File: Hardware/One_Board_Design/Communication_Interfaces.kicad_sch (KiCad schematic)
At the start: 51 parts, among them Q2 2SD882, Q5 2SD882, Q6 2SD882, U1 TCAN3414DR, U10 LTV-356T, U11 LTV-356T, U12 LTV-356T, U14 LTV-356T, U3 MAX3485, U6 LTV-356T

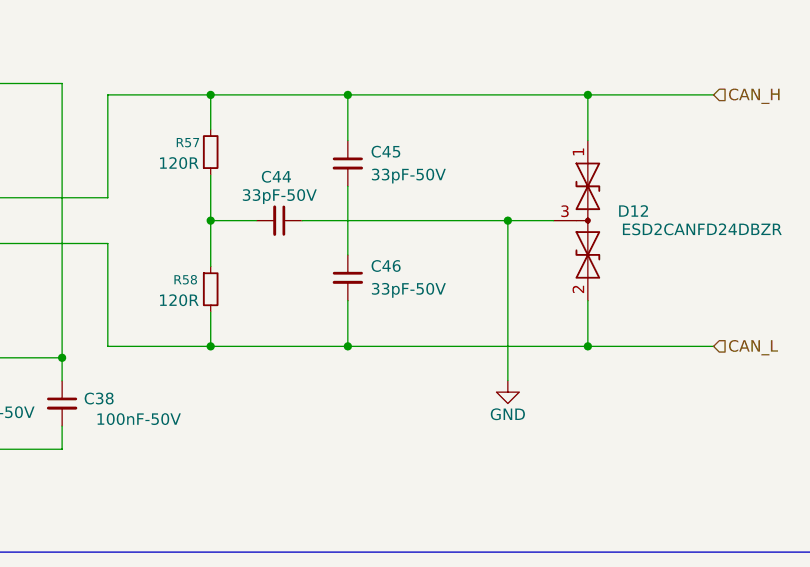
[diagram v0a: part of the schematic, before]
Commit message: refactor(hardware): move KiCad project into One_Board_Design/
Relocate the single-board KiCad project (root schematic, five hierarchical sheets, PCB, project file, and library tables) into Hardware/One_Board_Design/ so the shared symbols, footprints, and 3D models stay in Hardware/libraries/.

Update library tables and 3D model references to use \/../libraries/... so the moved project resolves the shared library location correctly. Replace SparkFun symbol references with the equivalent KiCad standard symbols. Add One_Board_Design README documenting the shared-library layout.

Ultraworked with [Sisyphus](https://github.com/code-yeongyu/oh-my-openagent)

Co-authored-by: Sisyphus <clio-agent@sisyphuslabs.ai>
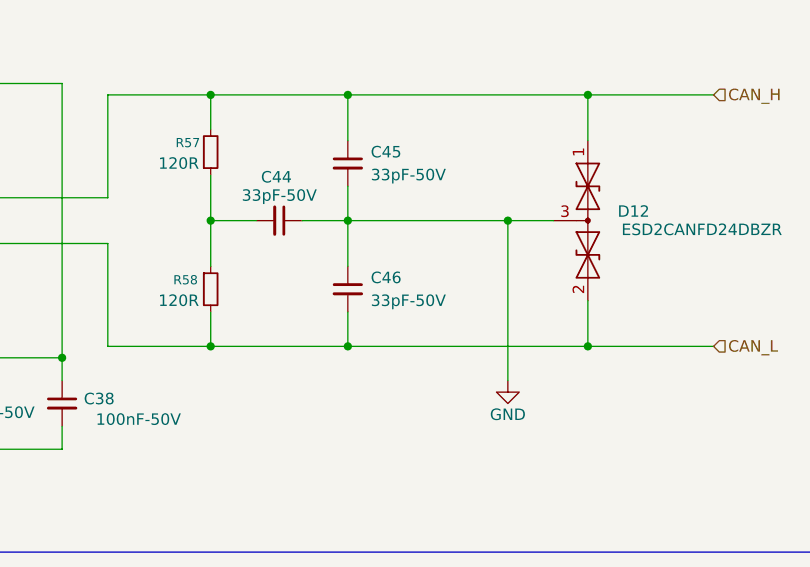
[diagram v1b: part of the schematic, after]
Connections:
- net GND: now also C45.2, C46.1
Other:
- moved on the sheet: C46
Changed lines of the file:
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@@
 	)
 	(junction
-		(at 215.9 58.42)
-		(diameter 0)
-		(color 0 0 0 0)
-	)
-	(junction
 		(at 160.02 97.79)
 		(diameter 0)
@@
 	)
 	(junction
+		(at 233.68 44.45)
+		(diameter 0)
+		(color 0 0 0 0)
+	)
+	(junction
 		(at 256.54 156.21)
 		(diameter 0)
@@
 	)
 	(junction
-		(at 233.68 44.45)
+		(at 82.55 99.06)
 		(diameter 0)
 		(color 0 0 0 0)
 	)
 	(junction
-		(at 82.55 99.06)
+		(at 215.9 58.42)
 		(diameter 0)
 		(color 0 0 0 0)
@@
 	)
 	(junction
+		(at 215.9 44.45)
+		(diameter 0)
+		(color 0 0 0 0)
+	)
+	(junction
 		(at 242.57 58.42)
 		(diameter 0)
@@
 	(wire
 		(pts
-			(xy 215.9 58.42) (xy 215.9 53.34)
+			(xy 215.9 58.42) (xy 215.9 54.61)
 		)
 		(stroke
@@
 	(wire
 		(pts
-			(xy 215.9 40.64) (xy 215.9 48.26)
-		)
-		(stroke
-			(width 0)
-			(type default)
-		)
-	)
-	(wire
-		(pts
 			(xy 161.29 158.75) (xy 161.29 161.29)
 		)
@@
 	(wire
 		(pts
-			(xy 233.68 44.45) (xy 233.68 62.23)
-		)
-		(stroke
-			(width 0)
-			(type default)
-		)
-	)
-	(wire
-		(pts
 			(xy 71.12 163.83) (xy 71.12 167.64)
 		)
@@
 	(wire
 		(pts
-			(xy 168.91 62.23) (xy 168.91 59.69)
+			(xy 233.68 44.45) (xy 238.76 44.45)
 		)
 		(stroke
@@
 	(wire
 		(pts
-			(xy 160.02 110.49) (xy 165.1 110.49)
+			(xy 168.91 62.23) (xy 168.91 59.69)
 		)
 		(stroke
@@
 	(wire
 		(pts
-			(xy 210.82 44.45) (xy 233.68 44.45)
+			(xy 160.02 110.49) (xy 165.1 110.49)
 		)
 		(stroke
@@
 	(wire
 		(pts
-			(xy 233.68 44.45) (xy 238.76 44.45)
+			(xy 210.82 44.45) (xy 215.9 44.45)
 		)
 		(stroke
@@
 	(wire
 		(pts
+			(xy 233.68 62.23) (xy 233.68 44.45)
+		)
+		(stroke
+			(width 0)
+			(type default)
+		)
+	)
+	(wire
+		(pts
 			(xy 48.26 30.48) (xy 48.26 34.29)
 		)
@@
 	(wire
 		(pts
+			(xy 215.9 44.45) (xy 233.68 44.45)
+		)
+		(stroke
+			(width 0)
+			(type default)
+		)
+	)
+	(wire
+		(pts
 			(xy 161.29 134.62) (xy 161.29 138.43)
 		)
@@
 	(wire
 		(pts
+			(xy 215.9 40.64) (xy 215.9 44.45)
+		)
+		(stroke
+			(width 0)
+			(type default)
+		)
+	)
+	(wire
+		(pts
 			(xy 226.06 140.97) (xy 234.95 140.97)
 		)
@@
 	(wire
 		(pts
+			(xy 215.9 44.45) (xy 215.9 49.53)
+		)
+		(stroke
+			(width 0)
+			(type default)
+		)
+	)
+	(wire
+		(pts
 			(xy 138.43 91.44) (xy 148.59 91.44)
 		)
@@
 	(symbol
 		(lib_id "Device:C_Small")
-		(at 215.9 50.8 0)
+		(at 215.9 52.07 0)
 		(unit 1)
 		(body_style 1)
@@
 		(dnp no)
 		(property "Reference" "C46"
-			(at 218.44 49.5362 0)
+			(at 218.44 50.8062 0)
 			(show_name no)
 			(do_not_autoplace no)
@@
 		)
 		(property "Value" "33pF-50V"
-			(at 218.44 52.0762 0)
+			(at 218.44 53.3462 0)
 			(show_name no)
 			(do_not_autoplace no)
@@
 		)
 		(property "Footprint" "Capacitor_SMD:C_0603_1608Metric"
-			(at 215.9 50.8 0)
+			(at 215.9 52.07 0)
 			(hide yes)
 			(show_name no)
@@
 		)
 		(property "Datasheet" ""
-			(at 215.9 50.8 0)
+			(at 215.9 52.07 0)
 			(hide yes)
 			(show_name no)
@@
 		)
 		(property "Description" "Unpolarized capacitor, small symbol"
-			(at 215.9 50.8 0)
+			(at 215.9 52.07 0)
 			(hide yes)
 			(show_name no)
@@
 		)
 		(property "BOM Comments" ""
-			(at 215.9 50.8 0)
+			(at 215.9 52.07 0)
 			(hide yes)
 			(show_name no)
@@
 		)
 		(property "DigiKey_Part_Number" ""
-			(at 215.9 50.8 0)
+			(at 215.9 52.07 0)
 			(hide yes)
 			(show_name no)
@@
 		)
 		(property "Link" ""
-			(at 215.9 50.8 0)
+			(at 215.9 52.07 0)
 			(hide yes)
 			(show_name no)
@@
 		)
 		(property "Sim.Type" ""
-			(at 215.9 50.8 0)
+			(at 215.9 52.07 0)
 			(hide yes)
 			(show_name no)
@@
 		)
 		(property "VENDOR" ""
-			(at 215.9 50.8 0)
+			(at 215.9 52.07 0)
 			(hide yes)
 			(show_name no)
@@
 		)
 		(property "Link to Buy" "https://linhkien.cxtvn.com/3426-tu-330-33pf-0603-50v-20c.html"
-			(at 476.25 -1.27 0)
+			(at 476.25 0 0)
 			(hide yes)
 			(show_name no)
